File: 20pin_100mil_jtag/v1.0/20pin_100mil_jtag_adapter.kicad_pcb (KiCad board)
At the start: 2 copper layers, 14 x 27 mm, 49 parts, among them J1 Jumper, SW1 TACT_G, X1 JTAG-10, X2 JTAG-20

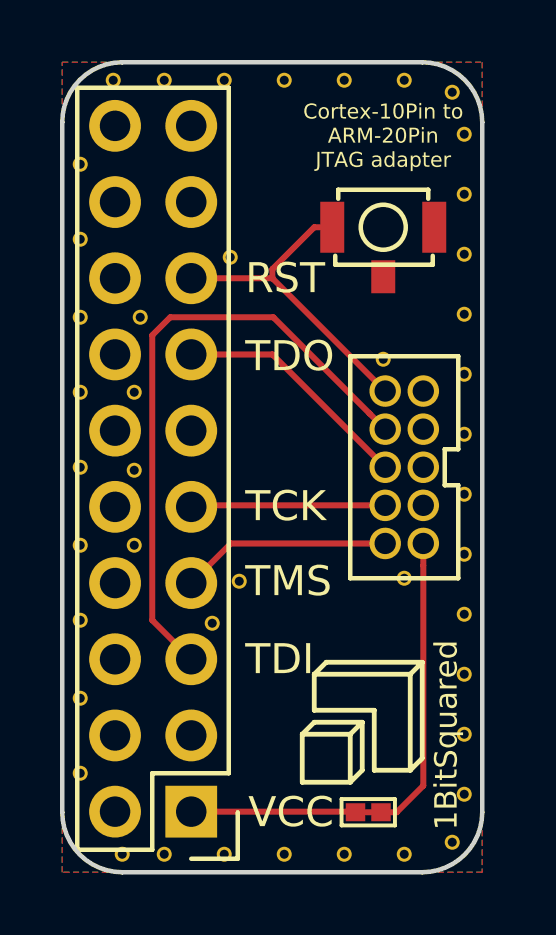
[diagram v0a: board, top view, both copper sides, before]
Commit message: Minor silkscreen cleanup.
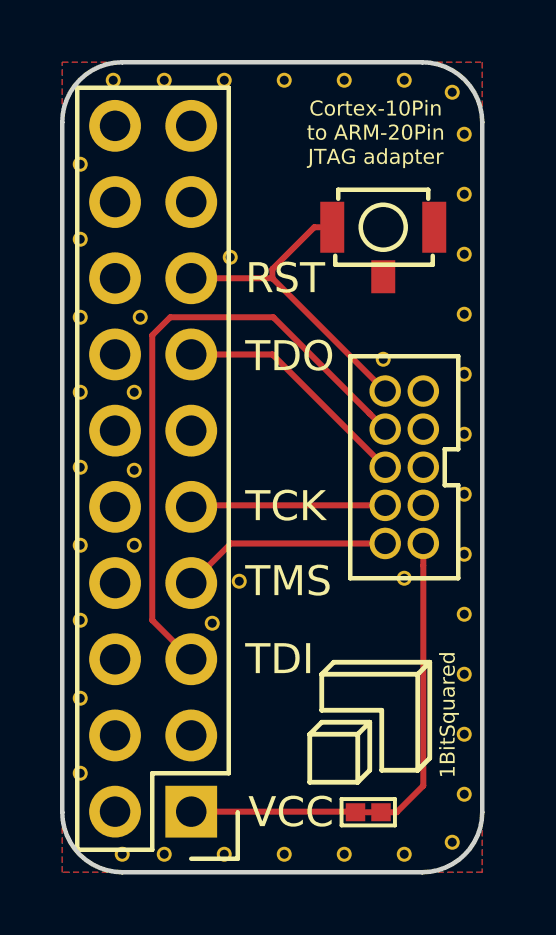
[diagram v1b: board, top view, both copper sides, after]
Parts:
- added REF**: 1b2_Logo_SilkS_4mm, pkl_logos:1b2_Logo_SilkS_4mm, B.Cu at (30.2, 42.0)
- moved REF** 0.25 mm to (30.2, 42.0)
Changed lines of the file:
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@@
-(kicad_pcb (version 4) (host pcbnew 4.0.1-4.201602132031+6195~38~ubuntu14.04.1-stable)
+(kicad_pcb (version 4) (host pcbnew 4.0.2-4+6225~38~ubuntu14.04.1-stable)
   (general
     (links 66)
@@
     (area 19.924999 19.924999 34.075001 47.075001)
     (thickness 1.6)
-    (drawings 33)
+    (drawings 34)
     (tracks 24)
     (zones 0)
-    (modules 49)
+    (modules 50)
     (nets 14)
   )
@@
     (add_net "Net-(X2-Pad3)")
   )
+  (module pkl_logos:1b2_Logo_SilkS_4mm (layer B.Cu)
+    (at 30.25 42 270)
+    (fp_text reference REF** (at 0 -3 270) (layer B.Fab) hide
+      (effects (font (size 1 1) (thickness 0.15)) (justify mirror))
+    )
+    (fp_text value 1b2_Logo_SilkS_4mm (at 0 3 270) (layer B.Fab) hide
+      (effects (font (size 1 1) (thickness 0.15)) (justify mirror))
+    )
+    (fp_line (start -1.2 -2) (end 2 -2) (layer B.SilkS) (width 0.16))
+    (fp_line (start -1.6 -1.6) (end -1.2 -2) (layer B.SilkS) (width 0.16))
+    (fp_line (start 2 -2) (end 1.6 -1.6) (layer B.SilkS) (width 0.16))
+    (fp_line (start 2 1.2) (end 2 -2) (layer B.SilkS) (width 0.16))
+    (fp_line (start 1.6 1.6) (end 2 1.2) (layer B.SilkS) (width 0.16))
+    (fp_line (start 1.6 -1.6) (end 1.6 1.6) (layer B.SilkS) (width 0.16))
+    (fp_line (start -1.6 -1.6) (end 1.6 -1.6) (layer B.SilkS) (width 0.16))
+    (fp_line (start -1.6 -0.4) (end -1.6 -1.6) (layer B.SilkS) (width 0.16))
+    (fp_line (start 0.4 -0.4) (end -1.6 -0.4) (layer B.SilkS) (width 0.16))
+    (fp_line (start 0.4 1.6) (end 0.4 -0.4) (layer B.SilkS) (width 0.16))
+    (fp_line (start 1.6 1.6) (end 0.4 1.6) (layer B.SilkS) (width 0.16))
+    (fp_line (start -1.6 0) (end 0 0) (layer B.SilkS) (width 0.16))
+    (fp_line (start -2 0.4) (end -1.6 0) (layer B.SilkS) (width 0.16))
+    (fp_line (start 0 0) (end -0.4 0.4) (layer B.SilkS) (width 0.16))
+    (fp_line (start 0 1.6) (end 0 0) (layer B.SilkS) (width 0.16))
+    (fp_line (start -0.4 2) (end 0 1.6) (layer B.SilkS) (width 0.16))
+    (fp_line (start -2 0.4) (end -0.4 0.4) (layer B.SilkS) (width 0.16))
+    (fp_line (start -2 2) (end -2 0.4) (layer B.SilkS) (width 0.16))
+    (fp_line (start -0.4 2) (end -2 2) (layer B.SilkS) (width 0.16))
+    (fp_line (start -0.4 0.4) (end -0.4 2) (layer B.SilkS) (width 0.16))
+  )
   (module pkl_misc:via0305 (layer F.Cu)
     (at 25.6 26.5)
@@
       (rotate (xyz 0 0 180))
     )
+    (model walter/conn_strip/vasch_strip_10x2.wrl
+      (at (xyz 0.45 -0.05 0))
+      (scale (xyz 1 1 1))
+      (rotate (xyz 180 0 0))
+    )
   )
   (module pkl_samtec:FTSH-105-XX-X-D (layer F.Cu)
@@
   )
   (module pkl_logos:1b2_Logo_SilkS_4mm (layer F.Cu)
-    (at 30 42 90)
+    (at 30.25 42 90)
     (fp_text reference REF** (at 0 3 90) (layer F.Fab) hide
       (effects (font (size 1 1) (thickness 0.15)))
@@
     )
   )
+  (gr_text 1BitSquared (at 32.85 42.25 90) (layer B.SilkS)
+    (effects (font (size 0.5 0.5) (thickness 0.125)) (justify mirror))
+  )
   (gr_line (start 20.5 46.25) (end 23 46.25) (layer F.SilkS) (width 0.15))
   (gr_line (start 20.5 20.85) (end 20.5 46.25) (layer F.SilkS) (width 0.15))
@@
     (effects (font (size 0.5 0.5) (thickness 0.125)) (justify mirror))
   )
-  (gr_text 1BitSquared (at 32.8 45.6 90) (layer F.SilkS)
-    (effects (font (size 0.75 0.75) (thickness 0.1875)) (justify left))
+  (gr_text 1BitSquared (at 32.85 41.75 90) (layer F.SilkS)
+    (effects (font (size 0.5 0.5) (thickness 0.125)))
   )
   (gr_text RST (at 26.1 27.2 180) (layer B.SilkS)
@@
     (effects (font (size 1 1) (thickness 0.25)) (justify left mirror))
   )
-  (gr_text TDI (at 26.2 39.9 180) (layer B.SilkS)
+  (gr_text TDI (at 25.75 39.9 180) (layer B.SilkS)
     (effects (font (size 1 1) (thickness 0.25)) (justify left mirror))
   )
@@
     (effects (font (size 1 1) (thickness 0.25)) (justify left))
   )
-  (gr_text "Cortex-10Pin to\nARM-20Pin\nJTAG adapter" (at 30.7 22.45) (layer F.SilkS)
+  (gr_text "Cortex-10Pin\nto ARM-20Pin\nJTAG adapter" (at 30.45 22.35) (layer F.SilkS)
     (effects (font (size 0.5 0.5) (thickness 0.125)))
   )

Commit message: Added pin 1 indicator on the 10pin connector.
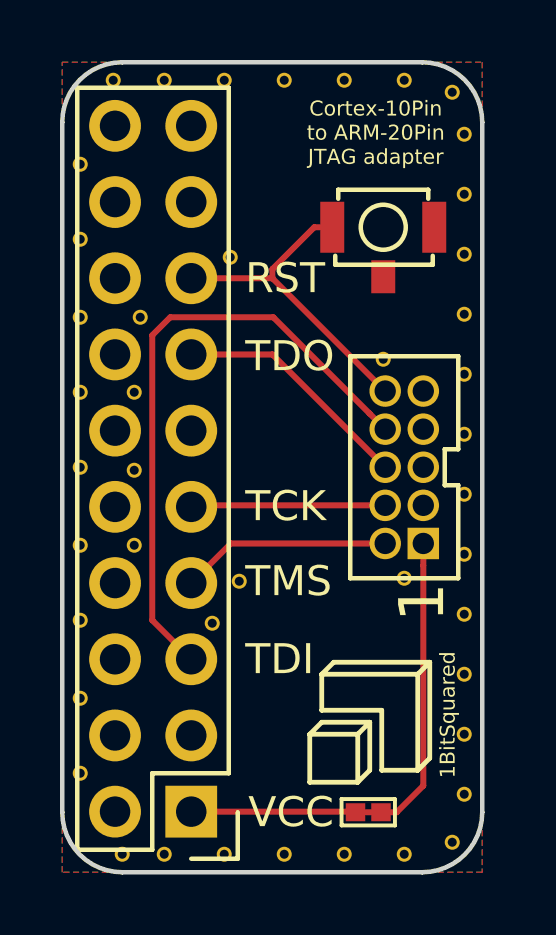
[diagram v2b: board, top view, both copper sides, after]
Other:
- board text added: "1"
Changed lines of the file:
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@@
-(kicad_pcb (version 4) (host pcbnew 4.0.2-4+6225~38~ubuntu14.04.1-stable)
+(kicad_pcb (version 4) (host pcbnew 4.0.7-e2-6376~58~ubuntu16.04.1)
   (general
     (links 66)
     (no_connects 0)
-    (area 19.924999 19.924999 34.075001 47.075001)
+    (area 16.325 15.3 43.85 50.176191)
     (thickness 1.6)
-    (drawings 34)
+    (drawings 35)
     (tracks 24)
     (zones 0)
@@
     (mod_text_size 1 1)
     (mod_text_width 0.15)
-    (pad_size 0.65 0.6)
-    (pad_drill 0)
+    (pad_size 1.05 1.05)
+    (pad_drill 0.71)
     (pad_to_mask_clearance 0.07)
     (aux_axis_origin 0 0)
@@
       (drillshape 0)
       (scaleselection 1)
-      (outputdirectory gerber))
+      (outputdirectory 20pin_jtag_gerber))
   )
   (net 0 "")
@@
     (pad 2 thru_hole circle (at -2.54 -0.635 90) (size 1.05 1.05) (drill 0.71) (layers *.Cu *.Mask F.SilkS)
       (net 8 /TMS))
-    (pad 1 thru_hole circle (at -2.54 0.635 90) (size 1.05 1.05) (drill 0.71) (layers *.Cu *.Mask F.SilkS)
+    (pad 1 thru_hole rect (at -2.54 0.635 90) (size 1.05 1.05) (drill 0.71) (layers *.Cu *.Mask F.SilkS)
       (net 9 /VCC))
     (pad 4 thru_hole circle (at -1.27 -0.635 90) (size 1.05 1.05) (drill 0.71) (layers *.Cu *.Mask F.SilkS)
@@
     )
   )
+  (gr_text 1 (at 32 38 90) (layer F.SilkS)
+    (effects (font (size 1.5 1.5) (thickness 0.3)))
+  )
   (gr_text 1BitSquared (at 32.85 42.25 90) (layer B.SilkS)
